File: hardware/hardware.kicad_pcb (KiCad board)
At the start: 2 copper layers, 12.6 x 19.1 mm, 9 parts, among them IC1 ATTINY1634-MU, P1 CONN_01X05, P2 CONN_01X05

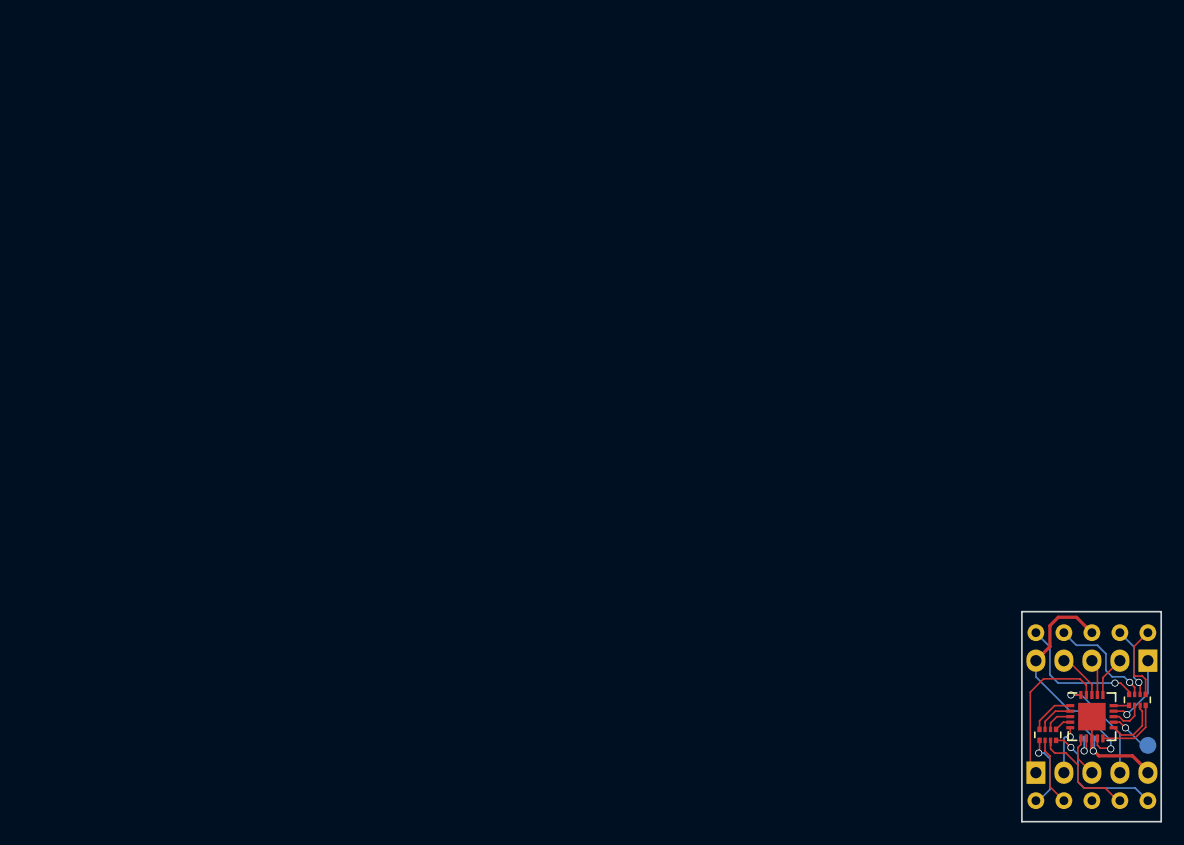
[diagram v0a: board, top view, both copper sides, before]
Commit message: * Redo layout to bring components to the bottom of the board.     ** Note this has changed the device pinout somewhat! * Bring everything into kicad 5 + Add kicad ignores.
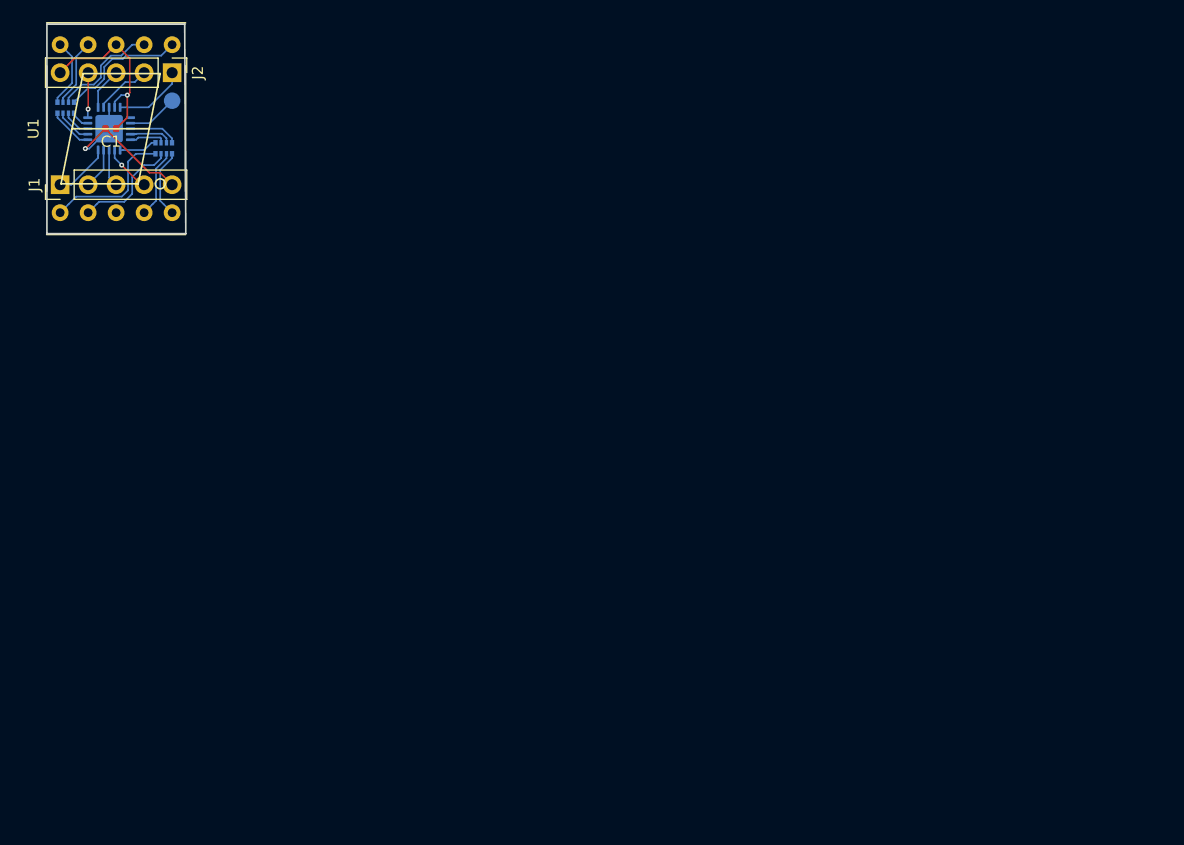
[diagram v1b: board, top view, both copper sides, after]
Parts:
- removed AFF1: 7SEGMENTS, seven-seg:7SegmentLED_LTS6760_LTS6780
- removed C2: 1u, Capacitors_SMD:C_0402
- removed P1, P2: CONN_01X05, seven-seg:Pin_Header_Straight_1x05
- removed RP1, RP2: 150, Resistors_SMD:R_Array_Convex_4x0402
- removed W1: TEST_1P, Measurement_Points:Measurement_Point_Round-SMD-Pad_Small
- added J1: Conn_01x05_Male, Connector_PinHeader_2.54mm:PinHeader_1x05_P2.54mm_Vertical, F.Cu at (101.6, 61.0)
- added J2: Conn_01x05_Male, Connector_PinHeader_2.54mm:PinHeader_1x05_P2.54mm_Vertical, F.Cu at (111.8, 50.8)
- added RN1: 150, Resistor_SMD:R_Array_Convex_4x0402, B.Cu at (111.0, 57.7)
- added RN2: 150, Resistor_SMD:R_Array_Convex_4x0402, B.Cu at (102.1, 54.0)
- added TP1: ~RESET, TestPoint:TestPoint_Pad_D1.5mm, B.Cu at (111.8, 53.3)
- added U1: KCSA02-105, Display_7Segment:7SegmentLED_LTS6760_LTS6780, F.Cu at (101.6, 63.5)
- C1: value 10n -> 1u; footprint Capacitors_SMD:C_0402 -> Capacitor_SMD:C_0402_1005Metric; moved to F.Cu
- IC1: footprint Housings_DFN_QFN:QFN-20-1EP_4x4mm_Pitch0.5mm -> Package_DFN_QFN:QFN-20-1EP_4x4mm_P0.5mm_EP2.5x2.5mm; moved to B.Cu
- moved C1 104.5 mm to (106.2, 55.9)
- moved IC1 103.9 mm to (106.0, 55.9)
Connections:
- C1 pad 1: GND -> +5V
- C1 pad 2: Net-(C1-Pad2) -> GND
- IC1 pad 10: ~SEG_B -> D3
- IC1 pad 11: ~SEG_A -> Net-(IC1-Pad11)
- IC1 pad 12: Net-(IC1-Pad12) -> /~RESET
- IC1 pad 13: ~SEG_F -> ~SEG_B
- IC1 pad 14: D3 -> ~SEG_A
- IC1 pad 15: ~SEG_G -> ~SEG_F
- IC1 pad 16: D2 -> ~SEG_G
- IC1 pad 17: D1 -> DEC
- IC1 pad 18: D0 -> DC_I
- IC1 pad 20: DC_I -> EN
- IC1 pad 5: EN -> D0
- IC1 pad 6: DEC -> D1
- IC1 pad 7: Net-(C1-Pad2) -> D2
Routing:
- net DC_O: track 14.2 -> 3.72 mm
- net DC_I: track 11.1 -> 3.41 mm, vias 1 -> 0
- net /DG: track 12.8 -> 6.21 mm, vias 1 -> 0
- net /DDP: track 12.8 -> 6.23 mm, vias 1 -> 0
- net /DE: track 6.89 -> 12.4 mm, vias 1 -> 0
- net +5V: track 22.0 -> 16.7 mm
- net /~RESET: track 0.00 -> 4.62 mm
- net /DB: track 7.29 -> 11.7 mm
- net /DF: track 10.4 -> 6.16 mm, vias 1 -> 0
- net Net-(IC1-Pad12): track 3.99 -> 0.00 mm, vias 1 -> 0
- net /DC: track 10.1 -> 6.18 mm
- net /DA: track 6.36 -> 9.90 mm, vias 1 -> 0
- net /DD: track 6.63 -> 9.95 mm
- net Net-(C1-Pad2): track 2.44 -> 0.00 mm, vias 1 -> 0
- net ~SEG_G: track 1.47 -> 3.48 mm
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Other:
- board size 12.6 x 19.1 mm -> 12.6 x 19 mm
- net class Default: via_dia 0.65 -> 0.45; via_drill 0.5 -> 0.2
- net class Power: trace_width 0.3 -> 0.1524; via_dia 0.65 -> 0.45; via_drill 0.5 -> 0.2
- rule via_min_drill: 0.5 -> 0.2
- rule via_min_size: 0.65 -> 0.45
- board text removed: "1"
- board text removed: "GB '17"
- board text removed: "~R"
